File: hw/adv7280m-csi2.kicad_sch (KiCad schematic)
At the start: 50 parts, among them J1 RPi_CSI_15pin, J2 CVBS_RCA, J3 CVBS_SMA, U1 ADV7280WBCPZ-M, U2 AP2112K-1.8, U3 AP2112K-1.8, Y1 28.63636MHz

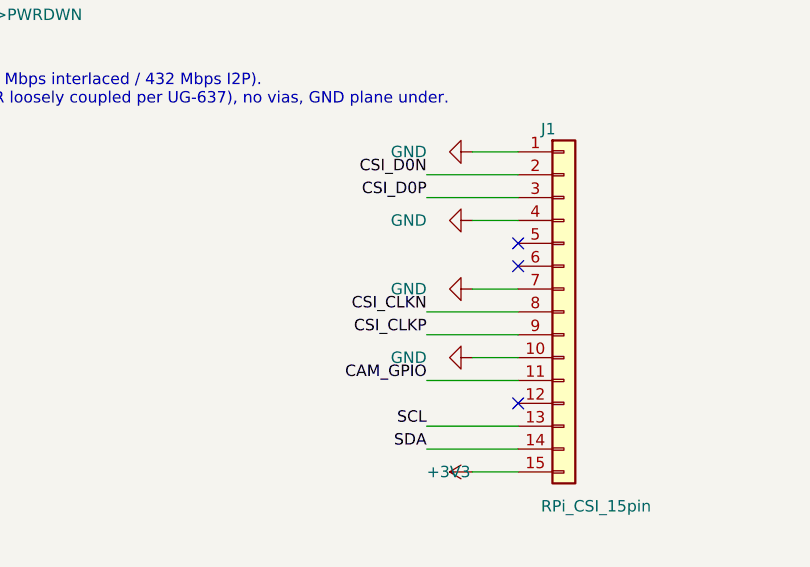
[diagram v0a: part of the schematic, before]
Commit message: Stage 1: tidy connector power-symbol labels, add schematic PNG preview
Co-Authored-By: Claude Fable 5.1 <noreply@anthropic.com>
Claude-Session: https://claude.ai/code/session_017Xy941kmWX9XJsHmZMcZcK
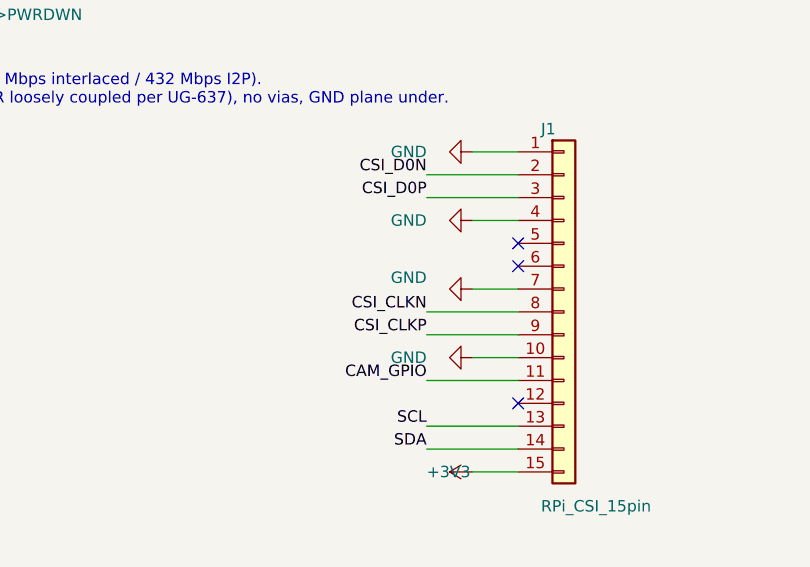
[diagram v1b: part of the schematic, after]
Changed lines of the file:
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@@
 		)
 		(property "Value" "GND"
-			(at 314.96 124.46 90)
+			(at 314.96 123.19 90)
 			(effects
 				(font

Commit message: Stage 2: 4-layer board, JLC04161H-7628 stackup, scripted placement, renders
- tools/gen_pcb.py builds the board from the schematic netlist: outline
  42x32 mm, layers, net classes (MIPI/Power), placement table, silkscreen
- FFC on the left edge (pin 1 top), CVBS RCA/SMA on the right edge,
  crystal and input network at the chip, LDOs bottom-left
- local SMA footprint without off-board silk; RCA/FFC silk fixes
- DRC: only unconnected items (routing is stage 3)
- docs/render-top.png, docs/render-bottom.png, assumptions stage 2

Co-Authored-By: Claude Fable 5.1 <noreply@anthropic.com>
Claude-Session: https://claude.ai/code/session_017Xy941kmWX9XJsHmZMcZcK
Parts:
- J3: footprint Connector_Coaxial:SMA_BAT_Wireless_BWSMA-KWE-Z001 -> adv-parts:SMA_BWSMA-KWE-Z001_EdgeMount
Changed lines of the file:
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@@
 			)
 		)
-		(property "Footprint" "Connector_Coaxial:SMA_BAT_Wireless_BWSMA-KWE-Z001"
+		(property "Footprint" "adv-parts:SMA_BWSMA-KWE-Z001_EdgeMount"
 			(at 116.84 121.92 0)
 			(effects

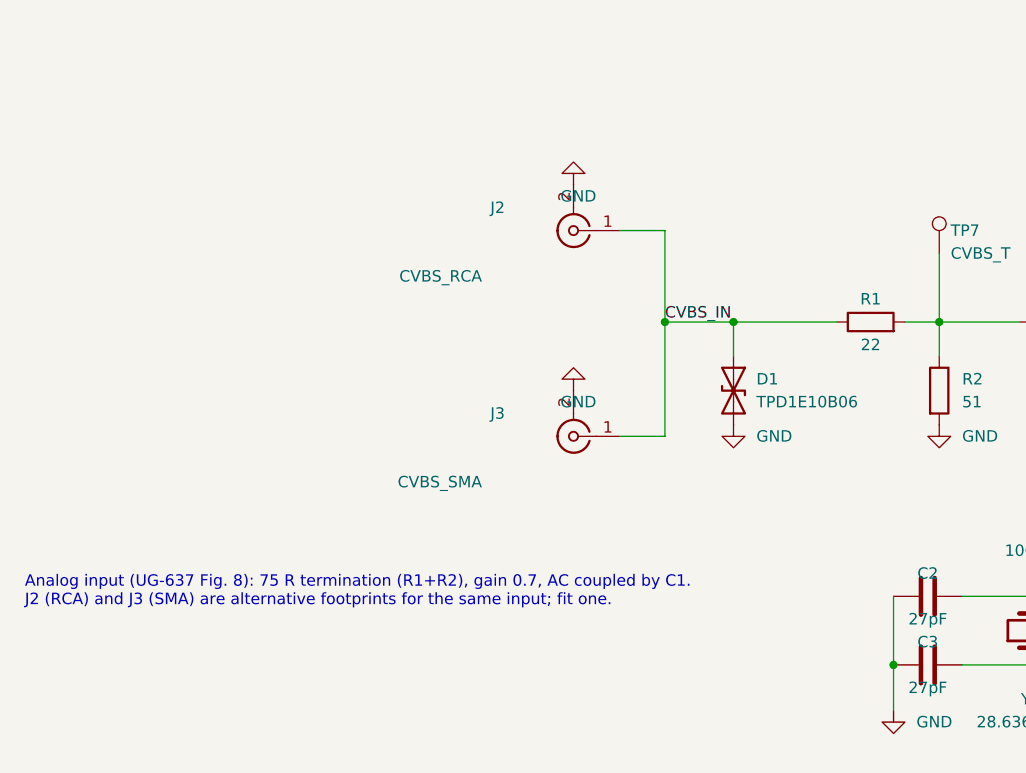
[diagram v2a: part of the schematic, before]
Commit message: Remove SMA input connector (J3): RCA only; regenerate schematic, board, docs
Co-Authored-By: Claude Fable 5.1 <noreply@anthropic.com>
Claude-Session: https://claude.ai/code/session_017Xy941kmWX9XJsHmZMcZcK
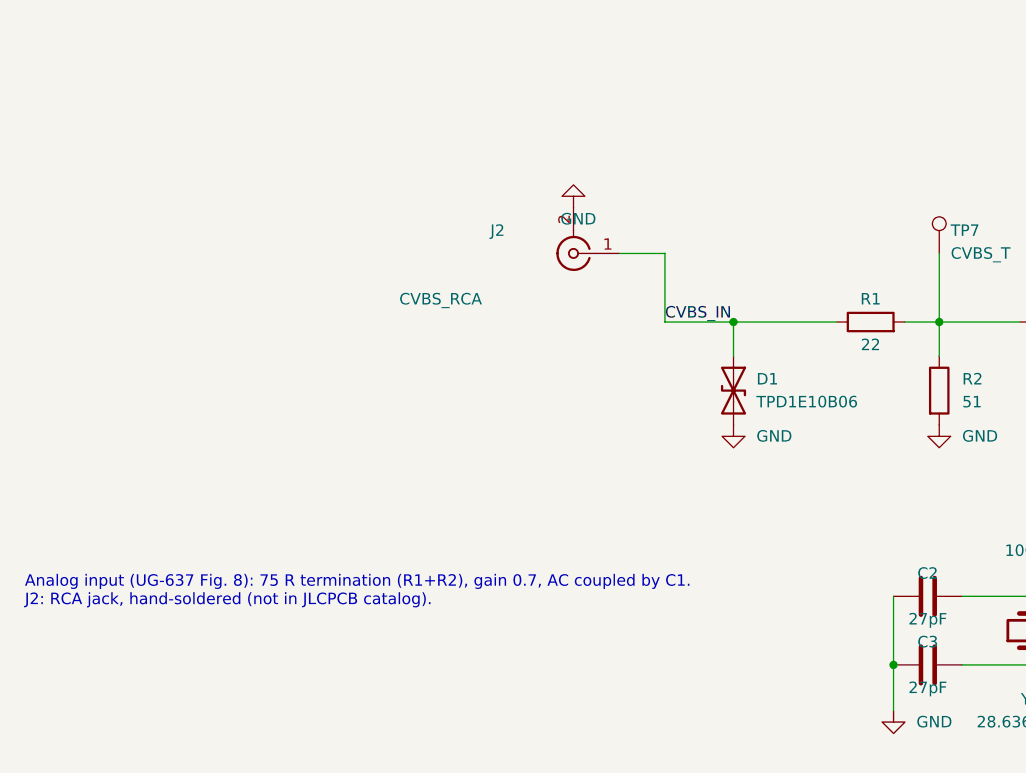
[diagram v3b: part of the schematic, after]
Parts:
- removed J3: CVBS_SMA, adv-parts:SMA_BWSMA-KWE-Z001_EdgeMount, symbol Connector:Conn_Coaxial
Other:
- note added: "Analog input (UG-637 Fig. 8): 75 R termination (R1+R2), gain 0.7, AC coupled by C1. J2: RCA jack, hand-soldered (not in JLCPCB catalog)."
- note removed: "Analog input (UG-637 Fig. 8): 75 R termination (R1+R2), gain 0.7, AC coupled by C1. J2 (RCA) and J3 (SMA) are alternative footprints for the same input; fit one."
- moved on the sheet: J2

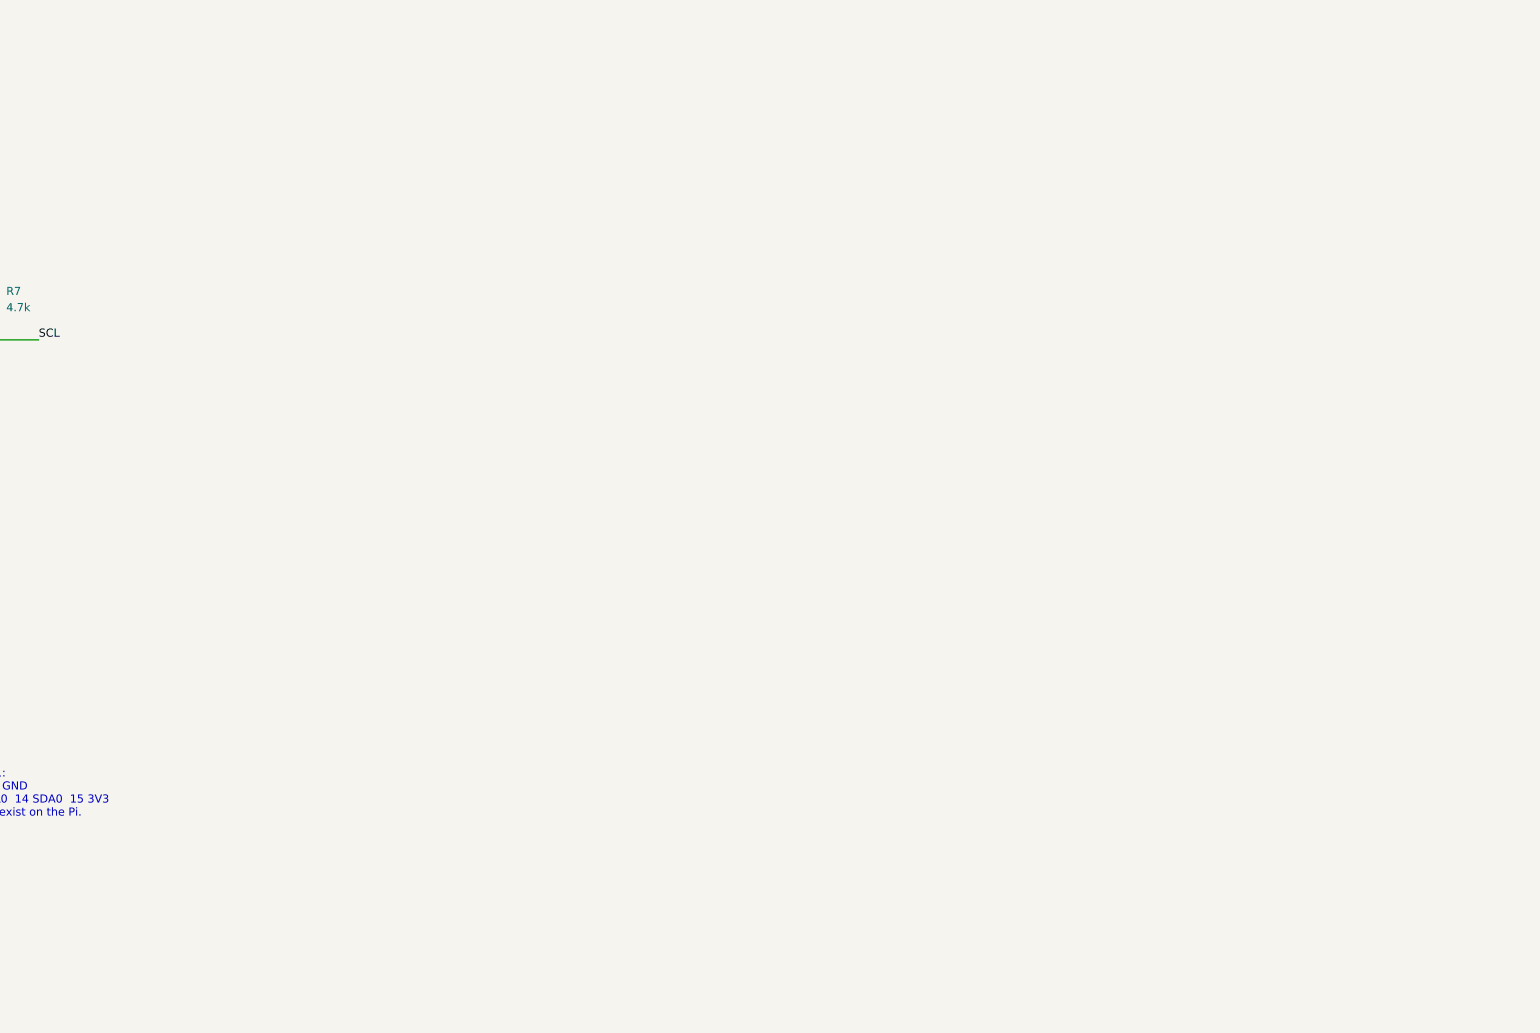
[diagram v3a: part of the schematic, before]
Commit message: Stage 5a: THS7314 buffer stage schematic (separable section), symbol, BOM, assumptions A5
- adv-parts library: THS7314 symbol (SLOS513A pinout)
- Schematic (A2, rev B): J4 screw terminal 5 V -> SS14 -> 22 uF -> ferrite -> THS7314 VS+;
  input header J5 with 75 R termination, ESD, 3 x 100 nF sync-tip-clamp coupling;
  outputs with 75 R back-termination: CH1 -> JP4 -> CVBS_IN (and J8 header), CH2/CH3 -> J6/J7
- ERC 0, check_nets extended, docs/schematic.pdf, schematic-1.png, bom.csv regenerated
- THS7314 datasheet added to docs/datasheets

Co-Authored-By: Claude Fable 5.1 <noreply@anthropic.com>
Claude-Session: https://claude.ai/code/session_017Xy941kmWX9XJsHmZMcZcK
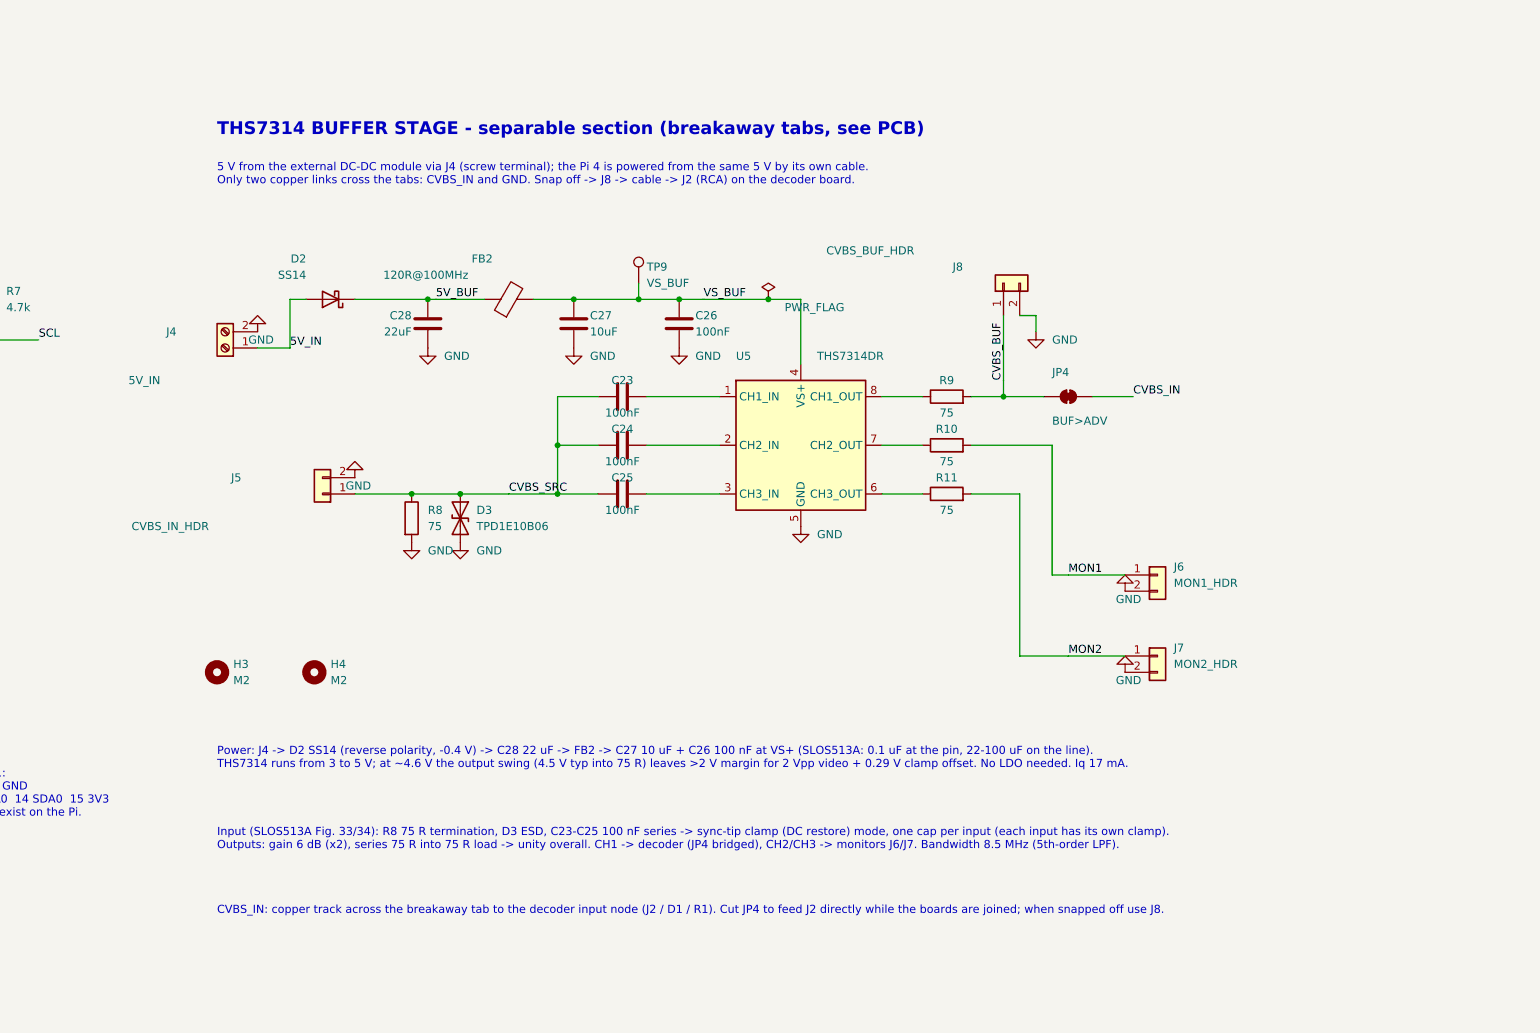
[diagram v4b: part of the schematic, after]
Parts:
- added C23, C24, C25: 100nF, Capacitor_SMD:C_0603_1608Metric, symbol Device:C
- added C26: 100nF, Capacitor_SMD:C_0402_1005Metric, symbol Device:C
- added C27: 10uF, Capacitor_SMD:C_0805_2012Metric, symbol Device:C
- added C28: 22uF, Capacitor_SMD:C_0805_2012Metric, symbol Device:C
- added D2: SS14, Diode_SMD:D_SMA, symbol Device:D_Schottky
- added D3: TPD1E10B06, adv-parts:TI_X1SON-2_DPY0002A_1.0x0.6mm, symbol Device:D_TVS
- added FB2: 120R@100MHz, Inductor_SMD:L_0603_1608Metric, symbol Device:FerriteBead
- added H3, H4: M2, MountingHole:MountingHole_2.2mm_M2, symbol Mechanical:MountingHole
- added J4: 5V_IN, TerminalBlock_Phoenix:TerminalBlock_Phoenix_MKDS-1,5-2-5.08_1x02_P5.08mm_Horizontal, symbol Connector:Screw_Terminal_01x02
- added J5: CVBS_IN_HDR, Connector_PinHeader_2.54mm:PinHeader_1x02_P2.54mm_Vertical, symbol Connector_Generic:Conn_01x02
- added J6: MON1_HDR, Connector_PinHeader_2.54mm:PinHeader_1x02_P2.54mm_Vertical, symbol Connector_Generic:Conn_01x02
- added J7: MON2_HDR, Connector_PinHeader_2.54mm:PinHeader_1x02_P2.54mm_Vertical, symbol Connector_Generic:Conn_01x02
- added J8: CVBS_BUF_HDR, Connector_PinHeader_2.54mm:PinHeader_1x02_P2.54mm_Vertical, symbol Connector_Generic:Conn_01x02
- added JP4: BUF>ADV, Jumper:SolderJumper-2_P1.3mm_Bridged_RoundedPad1.0x1.5mm, symbol Jumper:SolderJumper_2_Bridged
- added R10, R11, R8, R9: 75, Resistor_SMD:R_0603_1608Metric, symbol Device:R
- added TP9: VS_BUF, TestPoint:TestPoint_Pad_D1.5mm, symbol Connector:TestPoint
- added U5: THS7314DR, Package_SO:SOIC-8_3.9x4.9mm_P1.27mm, symbol adv-parts:THS7314
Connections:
- net CVBS_IN: now also JP4.2 (B)
- net GND: now also C26.2, C27.2, C28.2, D3.2 (A2), J4.2 (Pin_2), J5.2 (Pin_2), J6.2 (Pin_2), J7.2 (Pin_2), J8.2 (Pin_2), R8.2, U5.5 (GND)
- new net: C23.2, U5.1 (CH1_IN)
- new net: C24.2, U5.2 (CH2_IN)
- new net: C25.2, U5.3 (CH3_IN)
- new net: R11.1, U5.6 (CH3_OUT)
- new net: R10.1, U5.7 (CH2_OUT)
- new net: R9.1, U5.8 (CH1_OUT)
- new net 5V_BUF: C28.1, D2.1 (K), FB2.1
- new net 5V_IN: D2.2 (A), J4.1 (Pin_1)
- new net CVBS_BUF: J8.1 (Pin_1), JP4.1 (A), R9.2
- new net CVBS_SRC: C23.1, C24.1, C25.1, D3.1 (A1), J5.1 (Pin_1), R8.1
- new net MON1: J6.1 (Pin_1), R10.2
- new net MON2: J7.1 (Pin_1), R11.2
- new net VS_BUF: C26.1, C27.1, FB2.2, TP9.1, U5.4 (VS+)
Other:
- note added: "5 V from the external DC-DC module via J4 (screw terminal); the Pi 4 is powered from the same 5 V by its own cable. Only two copper links cross the tabs: CVBS_IN and GND. Snap off -> J8 -> cable -> J2 (RCA) on the decoder board."
- note added: "CVBS_IN: copper track across the breakaway tab to the decoder input node (J2 / D1 / R1). Cut JP4 to feed J2 directly while the boards are joined; when snapped off use J8."
- note added: "Input (SLOS513A Fig. 33/34): R8 75 R termination, D3 ESD, C23-C25 100 nF series -> sync-tip clamp (DC restore) mode, one cap per input (each input has its own clamp). Outputs: gain 6 dB (x2), series 75 R into 75 R load -> unity overall. CH1 -> decoder (JP4 bridged), CH2/CH3 -> monitors J6/J7. Bandwidth 8.5 MHz (5th-order LPF)."
- note added: "Power: J4 -> D2 SS14 (reverse polarity, -0.4 V) -> C28 22 uF -> FB2 -> C27 10 uF + C26 100 nF at VS+ (SLOS513A: 0.1 uF at the pin, 22-100 uF on the line). THS7314 runs from 3 to 5 V; at ~4.6 V the output swing (4.5 V typ into 75 R) leaves >2 V margin for 2 Vpp video + 0.29 V clamp offset. No LDO needed. Iq 17 mA."
- note added: "THS7314 BUFFER STAGE - separable section (breakaway tabs, see PCB)"
